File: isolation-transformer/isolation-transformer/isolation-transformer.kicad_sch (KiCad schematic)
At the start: 22 parts, among them J1 Conn_BNC_Vert_PCB, J2 Conn_BNC_Vert_PCB, J3 Conn_BNC_Vert_PCB, J4 Conn_BNC_Vert_PCB, T1 Hammond_560, T2 Hammond_560

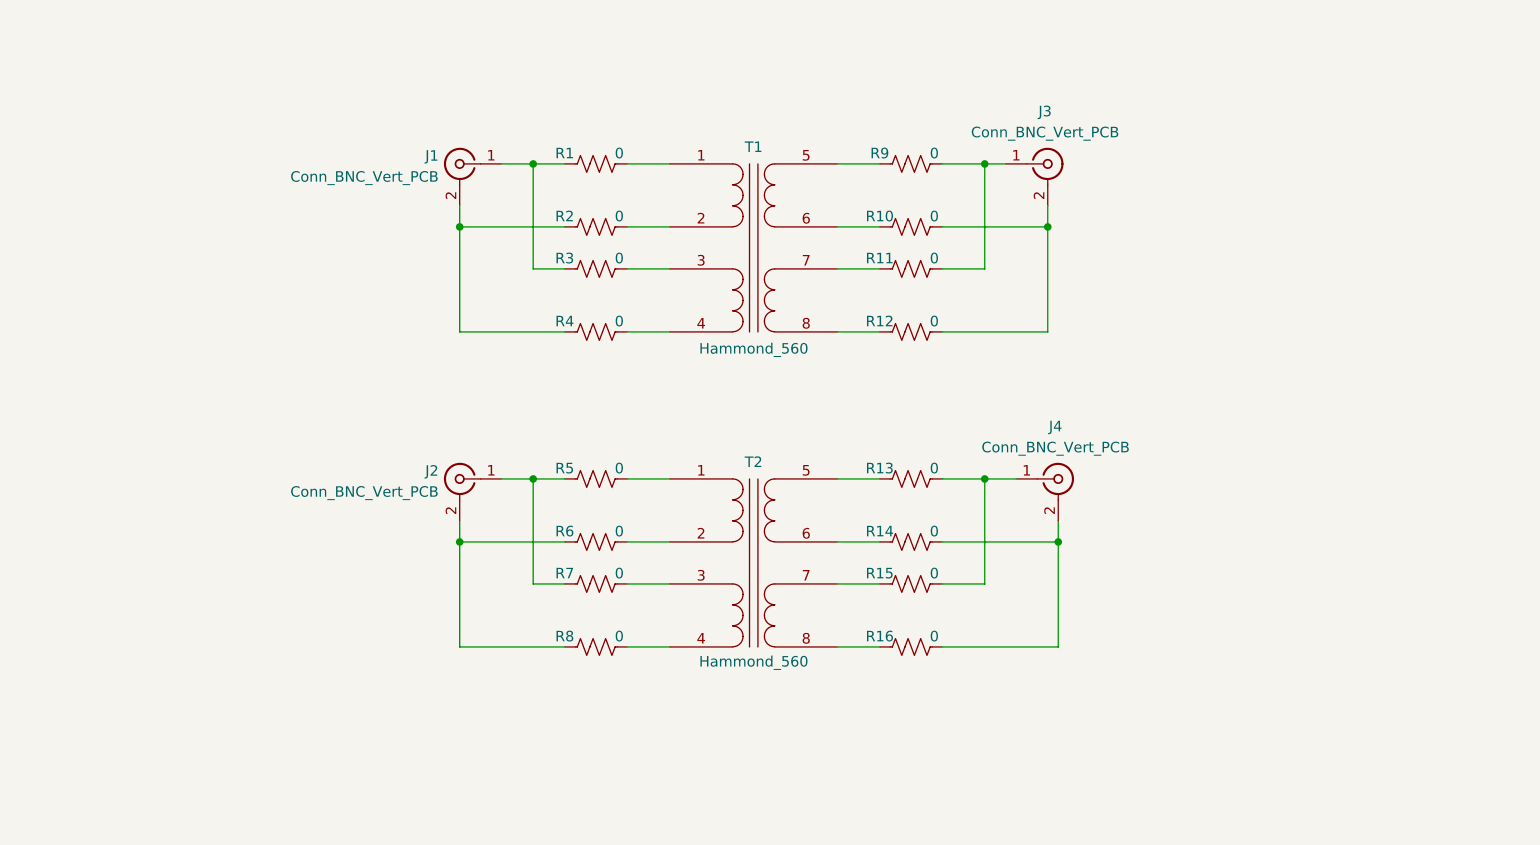
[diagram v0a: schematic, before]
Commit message: fix: add shield pin connect options
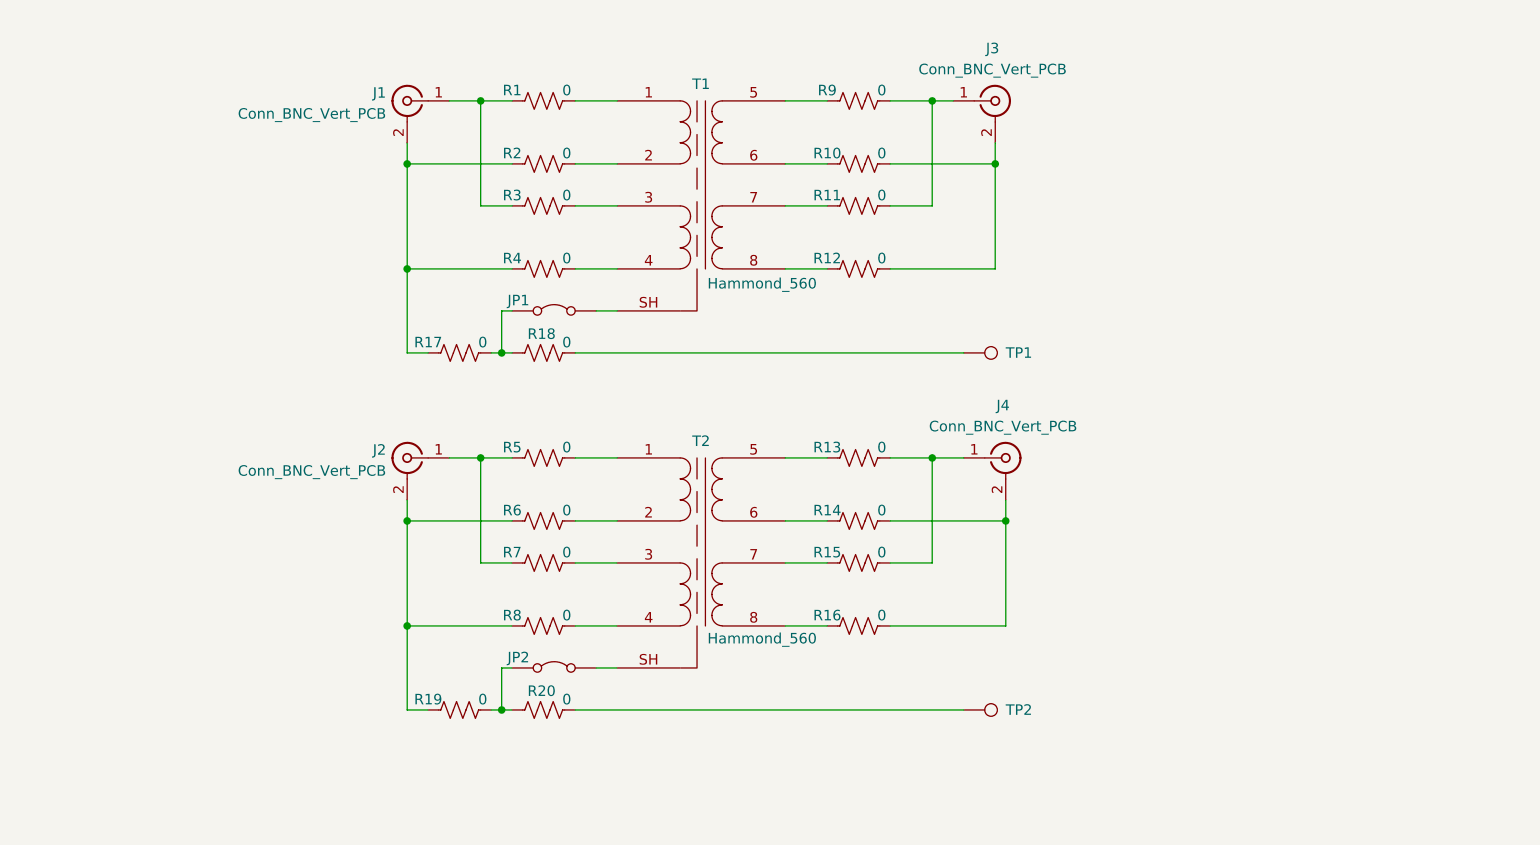
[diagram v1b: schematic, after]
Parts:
- added JP1, JP2: Jumper_2_Bridged, TestPoint:TestPoint_2Pads_Pitch2.54mm_Drill0.8mm, symbol Jumper:Jumper_2_Bridged
- added R17, R18, R19, R20: 0, Resistor_SMD:R_0603_1608Metric_Pad0.98x0.95mm_HandSolder, symbol Device:R_US
- added TP1, TP2: TestPoint, Connector_PinHeader_1.00mm:PinHeader_1x01_P1.00mm_Vertical, symbol Connector:TestPoint
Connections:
- net at J2.2 (Ext), R6.1, R8.1: now also R19.1
- net at J1.2 (Ext), R2.1, R4.1: now also R17.1
- new net: JP2.1 (A), R19.2, R20.1
- new net: JP2.2 (B), T2.SH (IN2B)
- new net: JP1.1 (A), R17.2, R18.1
- new net: JP1.2 (B), T1.SH (IN2B)
- new net: R18.2, TP1.1
- new net: R20.2, TP2.1
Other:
- moved on the sheet: J1, J2, J3, J4, R1, R10, R11, R12, R13, R14, R15, R16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

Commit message: feat: add 3D models and GND jmpr
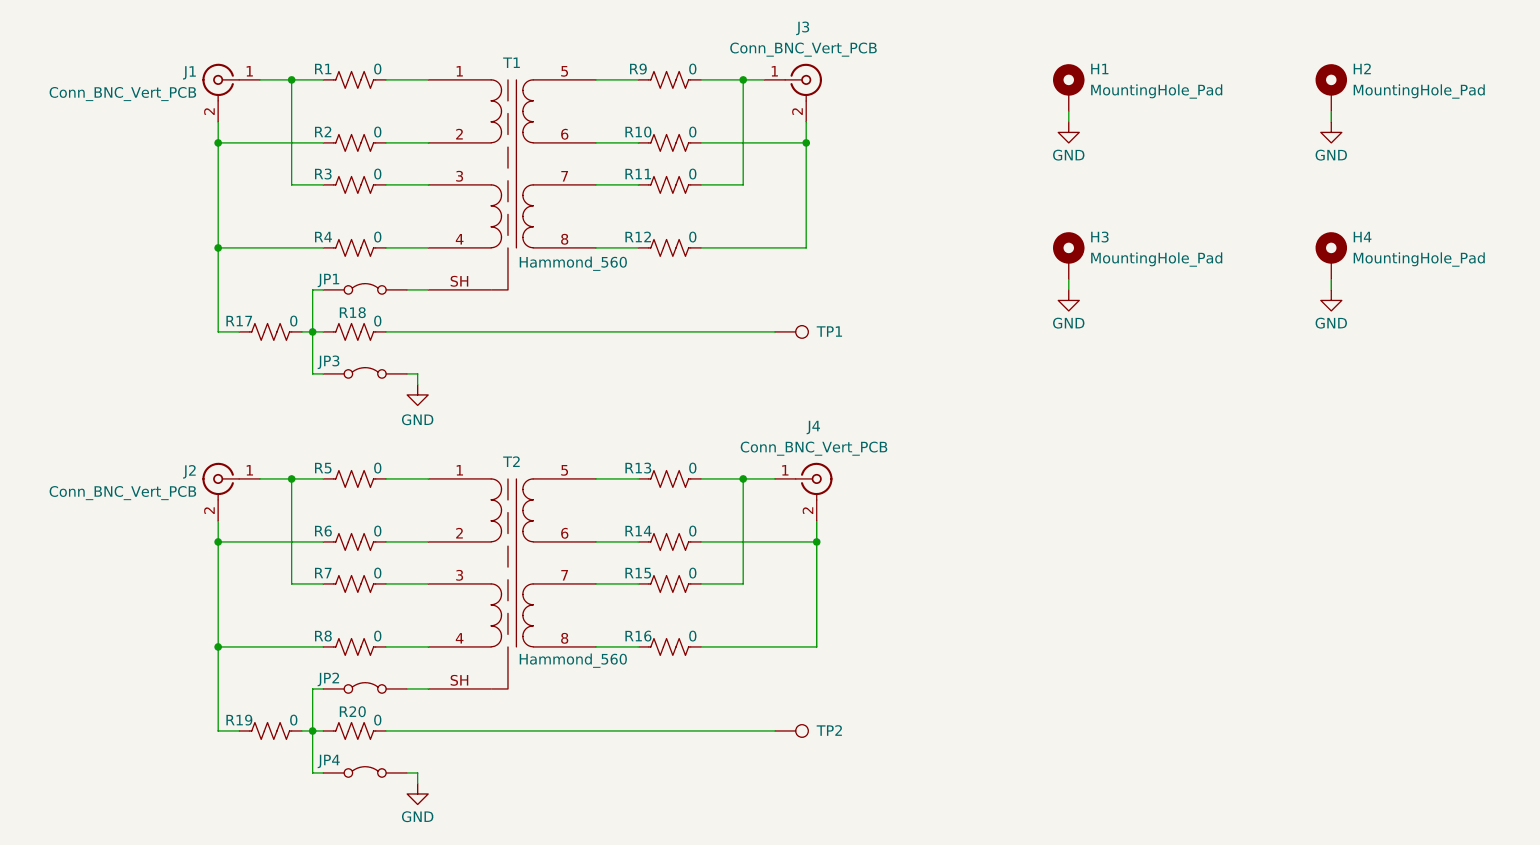
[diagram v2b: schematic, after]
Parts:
- added H1, H2, H3, H4: MountingHole_Pad, MountingHole:MountingHole_3.2mm_M3_Pad, symbol Mechanical:MountingHole_Pad
- added JP3, JP4: Jumper_2_Bridged, TestPoint:TestPoint_2Pads_Pitch2.54mm_Drill0.8mm, symbol Jumper:Jumper_2_Bridged
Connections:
- net at JP2.1 (A), R19.2, R20.1: now also JP4.1 (A)
- net at JP1.1 (A), R17.2, R18.1: now also JP3.1 (A)
- new net GND: H1.1, H2.1, H3.1, H4.1, JP3.2 (B), JP4.2 (B)
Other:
- moved on the sheet: J1, J2, J3, J4, JP1, JP2, R1, R10, R11, R12, R13, R14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
